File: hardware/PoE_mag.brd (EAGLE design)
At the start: 149.9 x 124.5 mm, 126 parts, among them IC1 LD1117V33, IC10 74LVC1T45SOT23-HAND, IC11 74LVC1T45SOT23-HAND, IC12 PCA9517A, IC2 LD1117V33, IC3 DS1338, IC4 ATMEGA1284, IC5 TSR 1-2450, IC6 LM61, IC7 MCP2200, IC8 74LVC1T45SOT23-HAND, IC9 74LVC1T45SOT23-HAND, Q1 BSS138, Q2 BUK98150-55A, X1 PWR, X2 JTAG, X3 USB, X4 MICRO-SD-SOCKETHIROSE-DM3D, X5 CONN-SMATHD, X6 UFL, X7 22-23-2021, X8 RJ45, X9 RJ11, Y1 32k768, Y2 12MHz, Y3 12MHz

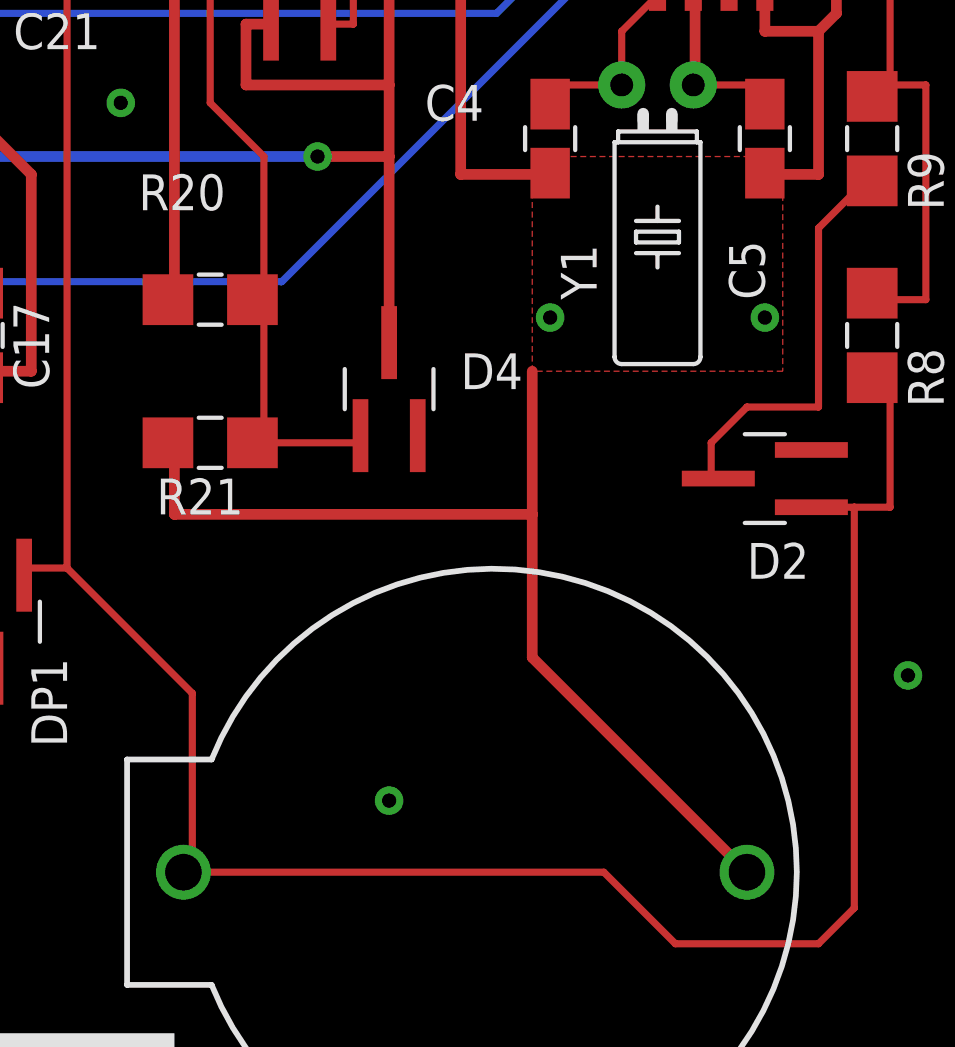
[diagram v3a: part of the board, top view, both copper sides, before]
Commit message: Add pads for support wire over 32768Hz crystal
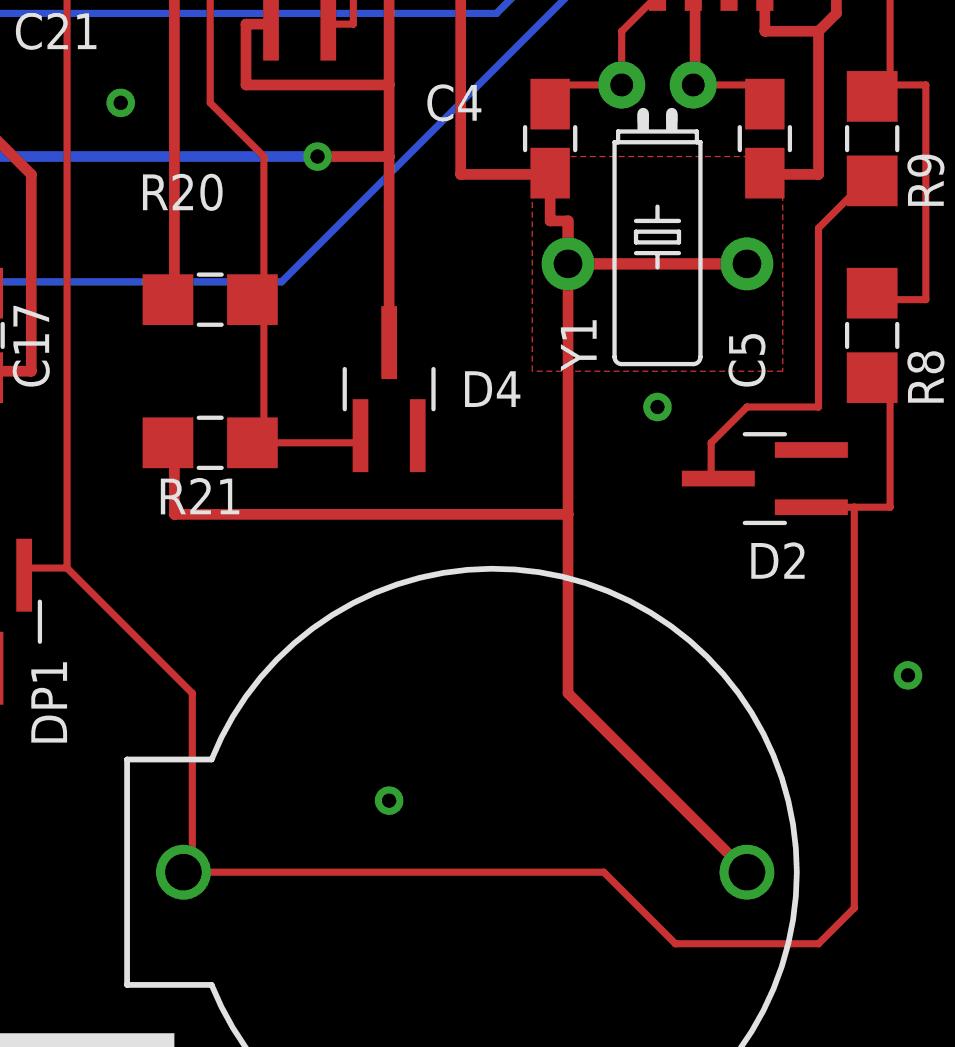
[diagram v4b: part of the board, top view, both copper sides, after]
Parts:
- added U$14, U$15: PAD, SteveMarple:PAD
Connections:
- net GND: now also U$14.1, U$15.1
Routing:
- net GND: track 1210.2 -> 1224.9 mm, vias 75 -> 74
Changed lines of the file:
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@@
 <rectangle x1="87.122" y1="1.524" x2="91.186" y2="2.794" layer="42"/>
 <text x="82.55" y="101.6" size="1.27" layer="25" ratio="10">PCB REV: 2</text>
+<wire x1="142.875" y1="24.765" x2="143.51" y2="23.495" width="0.254" layer="27"/>
+<wire x1="142.875" y1="24.765" x2="144.145" y2="23.495" width="0.254" layer="27"/>
+<wire x1="144.145" y1="24.13" x2="142.875" y2="24.765" width="0.254" layer="27"/>
+<wire x1="143.51" y1="23.495" x2="144.145" y2="24.13" width="0.254" layer="27"/>
+<wire x1="144.145" y1="23.495" x2="144.145" y2="22.225" width="0.254" layer="27"/>
 </plain>
 <attributes>
@@
 </class>
 </classes>
-<designrules name="SparkFun_Iteadstudio_10_12mil *">
+<designrules name="SparkFun_Iteadstudio_10_12mil">
 <description language="en">&lt;b&gt;EAGLE Design Rules&lt;/b&gt;
 &lt;p&gt;
@@
 </element>
 <element name="Y1" library="SteveMarple" package="TC38H" value="32k768" x="139.065" y="29.21" smashed="yes" rot="R180">
-<attribute name="NAME" x="136.906" y="21.59" size="1.27" layer="25" ratio="10" rot="R90"/>
+<attribute name="NAME" x="136.906" y="19.05" size="1.27" layer="25" ratio="10" rot="R90"/>
 </element>
 <element name="R2" library="SteveMarple" package="1206-HAND" value="560R" x="45.72" y="88.9" smashed="yes" rot="R270">
@@
 </element>
 <element name="C5" library="SteveMarple" package="0805-HAND" value="15p" x="142.875" y="27.305" smashed="yes" rot="R270">
-<attribute name="NAME" x="142.875" y="21.59" size="1.27" layer="25" ratio="10" rot="R90"/>
-<attribute name="VALUE" x="144.78" y="21.59" size="1.27" layer="27" ratio="10" rot="R90"/>
+<attribute name="NAME" x="142.875" y="18.415" size="1.27" layer="25" ratio="10" rot="R90"/>
+<attribute name="VALUE" x="144.78" y="18.415" size="1.27" layer="27" ratio="10" rot="R90"/>
 </element>
 <element name="C4" library="SteveMarple" package="0805-HAND" value="15p" x="135.255" y="27.305" smashed="yes" rot="R270">
@@
 </element>
 <element name="D4" library="SteveMarple" package="SOT23-3-HAND" value="BAS40" x="129.54" y="18.415" smashed="yes" rot="R90">
-<attribute name="NAME" x="132.08" y="18.415" size="1.27" layer="25" ratio="10" rot="SR0"/>
-<attribute name="VALUE" x="132.08" y="17.78" size="1.016" layer="27" ratio="10" rot="SR0" align="top-left"/>
+<attribute name="NAME" x="132.08" y="17.78" size="1.27" layer="25" ratio="10" rot="SR0"/>
+<attribute name="VALUE" x="132.08" y="16.51" size="1.016" layer="27" ratio="10" rot="SR0" align="top-left"/>
 </element>
 <element name="C41" library="SteveMarple" package="1206-HAND" value="100n" x="34.29" y="68.58" smashed="yes" rot="R270">
@@
 <attribute name="VALUE" x="72.39" y="10.16" size="1.27" layer="27" ratio="10"/>
 </element>
+<element name="U$14" library="SteveMarple" package="PAD" value="PAD" x="142.24" y="22.86"/>
+<element name="U$15" library="SteveMarple" package="PAD" value="PAD" x="135.89" y="22.86"/>
 </elements>
 <signals>
@@
 <wire x1="121.92" y1="16.51" x2="121.793" y2="16.637" width="0.381" layer="1"/>
 <wire x1="121.92" y1="13.97" x2="121.92" y2="16.51" width="0.381" layer="1"/>
-<wire x1="134.62" y1="13.97" x2="121.92" y2="13.97" width="0.381" layer="1"/>
-<wire x1="134.62" y1="19.05" x2="134.62" y2="13.97" width="0.381" layer="1"/>
+<wire x1="135.89" y1="13.97" x2="121.92" y2="13.97" width="0.381" layer="1"/>
+<wire x1="135.89" y1="22.86" x2="135.89" y2="13.97" width="0.381" layer="1"/>
 <wire x1="121.92" y1="16.51" x2="121.691" y2="16.51" width="0.381" layer="1"/>
 <wire x1="132.08" y1="33.655" x2="136.525" y2="33.655" width="0.381" layer="1"/>
@@
 <wire x1="132.08" y1="26.035" x2="132.08" y2="33.655" width="0.381" layer="1"/>
 <wire x1="135.128" y1="26.162" x2="135.255" y2="26.035" width="0.381" layer="1"/>
+<wire x1="135.255" y1="26.035" x2="135.255" y2="24.384" width="0.381" layer="1"/>
+<wire x1="135.255" y1="24.384" x2="135.89" y2="24.384" width="0.381" layer="1"/>
 <wire x1="135.255" y1="26.035" x2="132.08" y2="26.035" width="0.381" layer="1"/>
 <wire x1="136.398" y1="34.036" x2="136.525" y2="34.061" width="0.381" layer="1"/>
@@
 <wire x1="142.875" y1="26.035" x2="144.78" y2="26.035" width="0.381" layer="1"/>
 <wire x1="143.002" y1="26.162" x2="142.875" y2="26.08" width="0.381" layer="1"/>
-<wire x1="134.62" y1="8.89" x2="142.24" y2="1.27" width="0.381" layer="1"/>
-<wire x1="134.62" y1="13.97" x2="134.62" y2="8.89" width="0.381" layer="1"/>
+<wire x1="135.89" y1="7.62" x2="142.24" y2="1.27" width="0.381" layer="1"/>
+<wire x1="135.89" y1="13.97" x2="135.89" y2="7.62" width="0.381" layer="1"/>
 <wire x1="132.08" y1="33.655" x2="126.365" y2="33.655" width="0.381" layer="16"/>
 <wire x1="60.96" y1="24.765" x2="61.366" y2="24.765" width="0.6096" layer="1"/>
@@
 <via x="140.335" y="60.325" extent="1-16" drill="0.508"/>
 <via x="135.255" y="62.865" extent="1-16" drill="0.508"/>
-<via x="135.255" y="20.955" extent="1-16" drill="0.508"/>
-<via x="142.875" y="20.955" extent="1-16" drill="0.508"/>
 <via x="113.03" y="19.05" extent="1-16" drill="0.508"/>
 <via x="31.75" y="63.5" extent="1-16" drill="0.508"/>
@@
 <wire x1="63.5" y1="96.52" x2="63.754" y2="96.52" width="0.381" layer="1"/>
 <via x="102.87" y="101.6" extent="1-16" drill="0.508"/>
+<via x="139.065" y="17.78" extent="1-16" drill="0.508"/>
+<contactref element="U$14" pad="1"/>
+<contactref element="U$15" pad="1"/>
+<wire x1="142.24" y1="22.86" x2="135.89" y2="22.86" width="0.4064" layer="1"/>
+<wire x1="135.89" y1="22.86" x2="135.89" y2="24.384" width="0.4064" layer="1"/>
 </signal>
 <signal name="VCC" class="1">

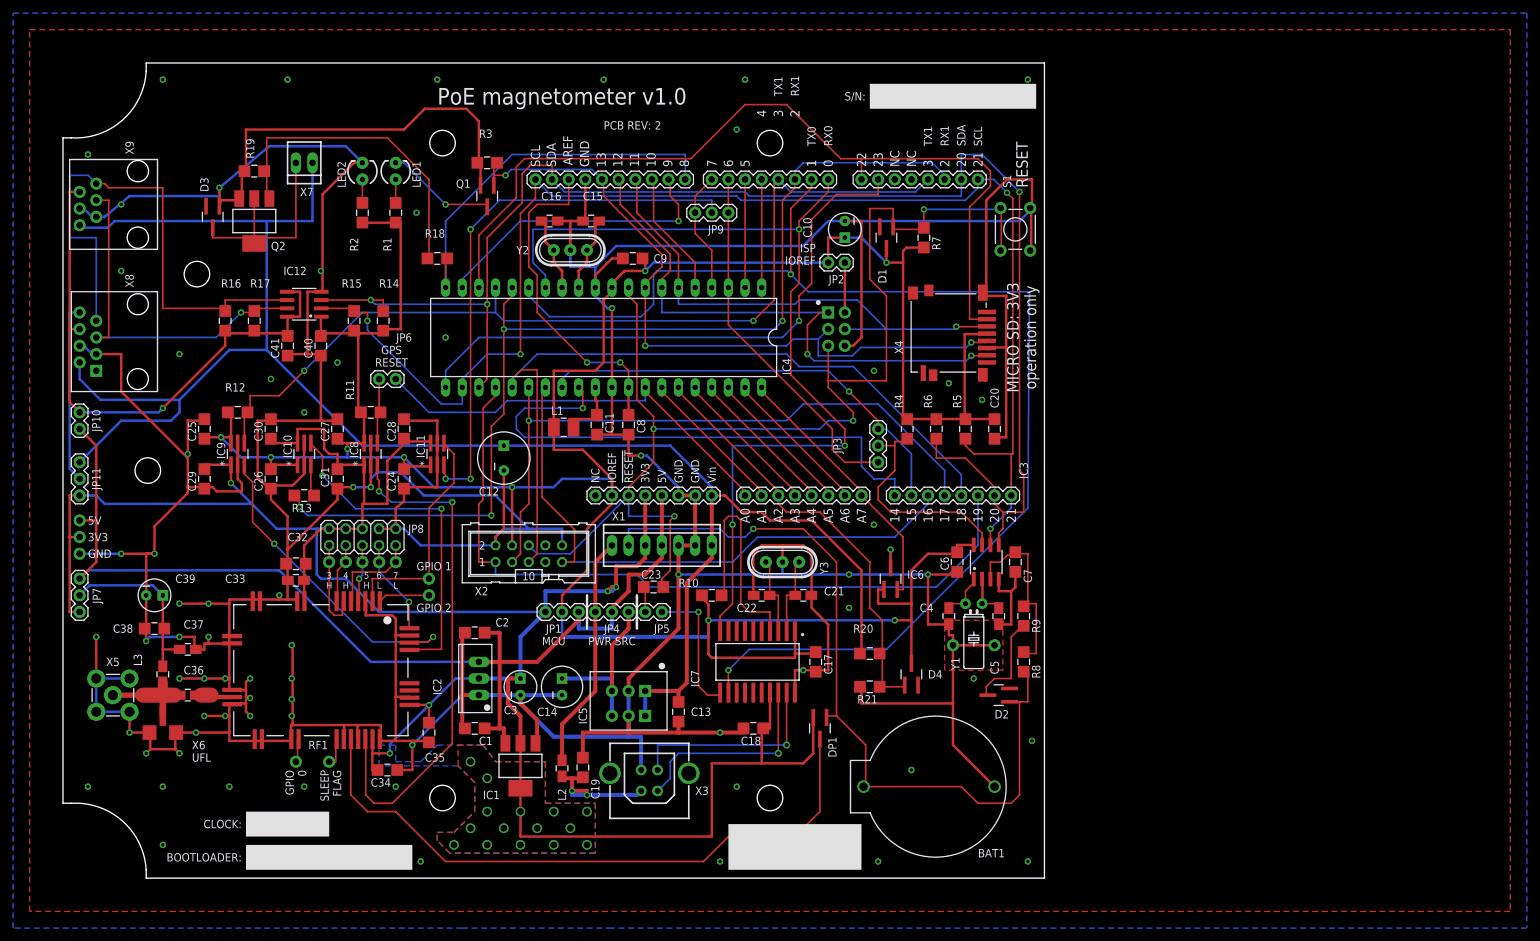
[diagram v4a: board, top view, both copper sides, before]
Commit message: Reroute bottom layer tracks to avoid lugs on box
Also use 4mm diameter mounting holes
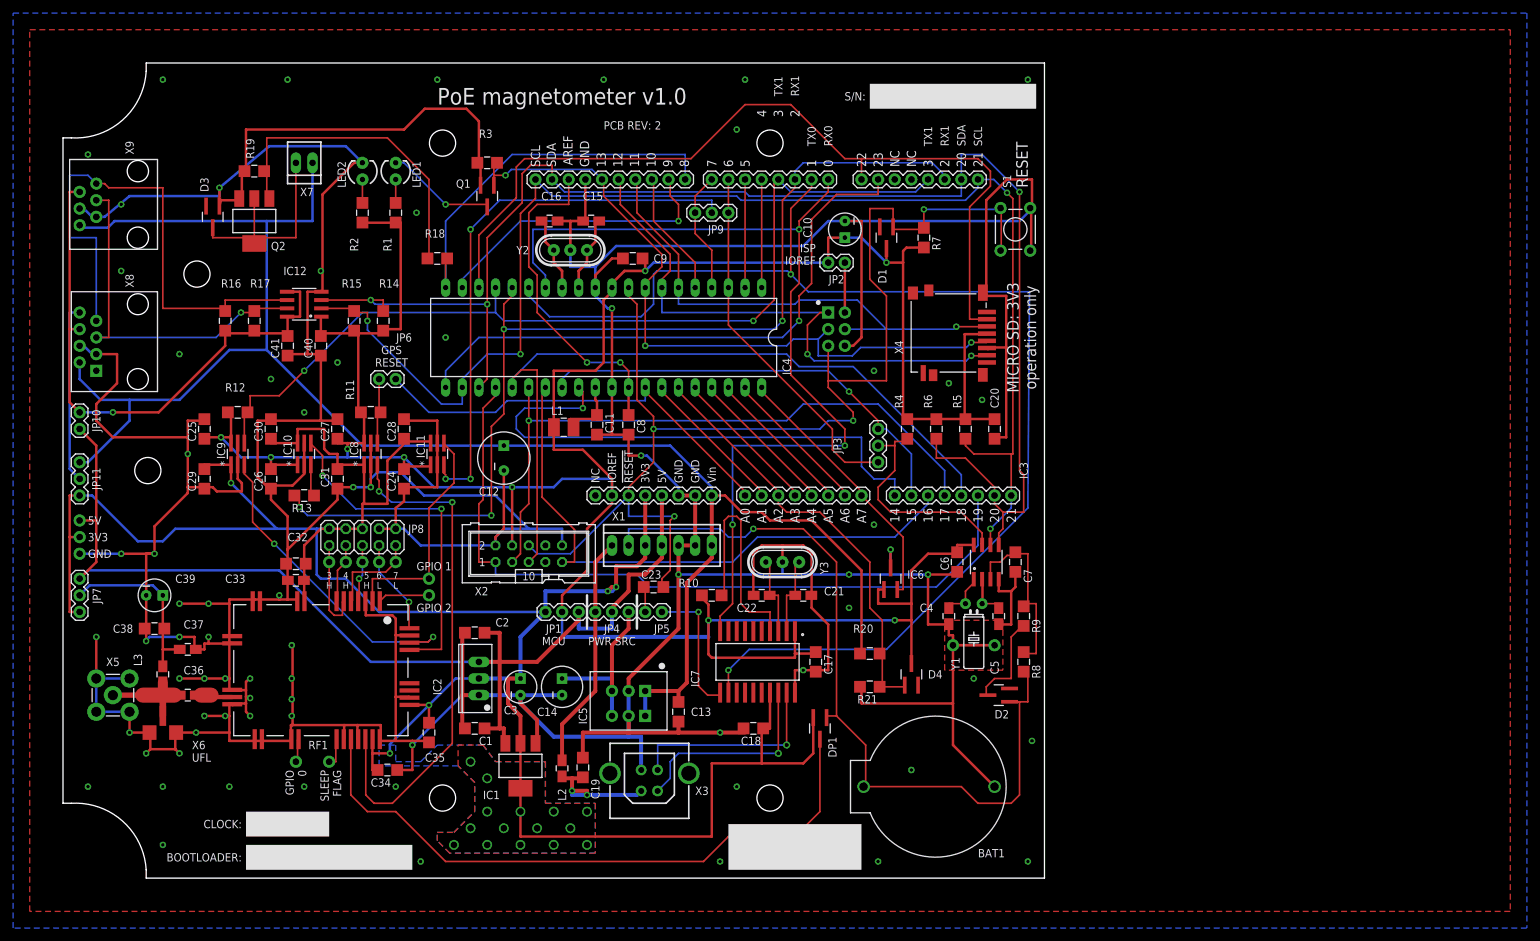
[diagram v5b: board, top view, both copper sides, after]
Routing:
- net +3V3: track 375.6 -> 382.6 mm
- net VIN: track 278.1 -> 271.2 mm
- net GND: track 1224.9 -> 1230.7 mm
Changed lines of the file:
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@@
 <wire x1="27.305" y1="47.625" x2="27.305" y2="46.355" width="0.381" layer="1"/>
 <wire x1="19.05" y1="57.15" x2="21.59" y2="57.15" width="0.381" layer="1"/>
-<wire x1="19.05" y1="46.99" x2="19.05" y2="51.435" width="0.381" layer="1"/>
-<wire x1="19.05" y1="51.435" x2="19.05" y2="57.15" width="0.381" layer="1"/>
+<wire x1="19.05" y1="46.99" x2="19.05" y2="54.61" width="0.381" layer="1"/>
+<wire x1="19.05" y1="54.61" x2="19.05" y2="57.15" width="0.381" layer="1"/>
 <wire x1="19.05" y1="46.99" x2="19.05" y2="46.101" width="0.381" layer="1"/>
 <wire x1="21.59" y1="57.15" x2="21.59" y2="57.379" width="0.381" layer="1"/>
 <wire x1="26.67" y1="50.419" x2="26.67" y2="53.721" width="0.381" layer="1"/>
-<wire x1="8.89" y1="67.31" x2="5.08" y2="67.31" width="0.381" layer="1"/>
-<wire x1="8.89" y1="61.595" x2="8.89" y2="67.31" width="0.381" layer="1"/>
-<wire x1="19.05" y1="51.435" x2="8.89" y2="61.595" width="0.381" layer="1"/>
+<wire x1="8.255" y1="67.31" x2="5.08" y2="67.31" width="0.381" layer="1"/>
+<wire x1="7.62" y1="54.61" x2="5.08" y2="57.15" width="0.381" layer="1"/>
+<wire x1="5.08" y1="57.15" x2="5.08" y2="59.69" width="0.381" layer="1"/>
+<wire x1="5.08" y1="59.69" x2="8.255" y2="62.865" width="0.381" layer="1"/>
+<wire x1="8.255" y1="62.865" x2="8.255" y2="67.31" width="0.381" layer="1"/>
+<wire x1="19.05" y1="54.61" x2="7.62" y2="54.61" width="0.381" layer="1"/>
 <wire x1="13.97" y1="36.83" x2="8.89" y2="36.83" width="0.381" layer="1"/>
 <wire x1="13.97" y1="36.83" x2="13.97" y2="41.021" width="0.381" layer="1"/>
@@
 <wire x1="95.885" y1="97.155" x2="70.485" y2="97.155" width="0.254" layer="1"/>
 <wire x1="104.14" y1="105.41" x2="95.885" y2="97.155" width="0.254" layer="1"/>
-<wire x1="121.92" y1="97.155" x2="118.745" y2="97.155" width="0.254" layer="1"/>
-<wire x1="118.745" y1="97.155" x2="110.49" y2="105.41" width="0.254" layer="1"/>
-<wire x1="110.49" y1="105.41" x2="104.14" y2="105.41" width="0.254" layer="1"/>
+<wire x1="121.92" y1="97.155" x2="119.38" y2="97.155" width="0.254" layer="1"/>
+<wire x1="119.38" y1="97.155" x2="111.125" y2="105.41" width="0.254" layer="1"/>
+<wire x1="111.125" y1="105.41" x2="104.14" y2="105.41" width="0.254" layer="1"/>
 </signal>
 <signal name="9">
@@
 <wire x1="43.18" y1="40.64" x2="45.72" y2="40.64" width="0.381" layer="1"/>
 <wire x1="25.654" y1="47.625" x2="25.654" y2="50.419" width="0.381" layer="1"/>
-<wire x1="32.639" y1="40.64" x2="28.829" y2="44.45" width="0.381" layer="16"/>
-<wire x1="28.829" y1="44.45" x2="25.654" y2="47.625" width="0.381" layer="16"/>
+<wire x1="32.639" y1="40.64" x2="25.654" y2="47.625" width="0.381" layer="16"/>
 <wire x1="40.64" y1="40.64" x2="38.735" y2="40.64" width="0.381" layer="16"/>
 <wire x1="38.735" y1="40.64" x2="32.639" y2="40.64" width="0.381" layer="16"/>
@@
 <wire x1="36.83" y1="38.1" x2="36.83" y2="35.56" width="0.381" layer="1"/>
 <wire x1="36.83" y1="35.56" x2="37.059" y2="35.306" width="0.381" layer="1"/>
-<wire x1="28.829" y1="44.45" x2="6.35" y2="44.45" width="0.381" layer="16"/>
-<wire x1="6.35" y1="44.45" x2="5.08" y2="45.72" width="0.381" layer="16"/>
-<wire x1="5.08" y1="45.72" x2="2.54" y2="45.72" width="0.381" layer="16"/>
+<wire x1="32.639" y1="40.64" x2="17.145" y2="40.64" width="0.381" layer="16"/>
+<wire x1="17.145" y1="40.64" x2="15.24" y2="38.735" width="0.381" layer="16"/>
+<wire x1="15.24" y1="38.735" x2="11.43" y2="38.735" width="0.381" layer="16"/>
+<wire x1="11.43" y1="38.735" x2="4.445" y2="45.72" width="0.381" layer="16"/>
+<wire x1="4.445" y1="45.72" x2="2.54" y2="45.72" width="0.381" layer="16"/>
 <wire x1="113.03" y1="4.826" x2="114.554" y2="6.35" width="0.381" layer="1"/>
 <wire x1="106.68" y1="4.826" x2="113.03" y2="4.826" width="0.381" layer="1"/>
@@
 <wire x1="99.06" y1="38.1" x2="99.06" y2="36.195" width="0.6096" layer="1"/>
 <wire x1="99.06" y1="36.195" x2="95.25" y2="32.385" width="0.6096" layer="1"/>
-<wire x1="8.89" y1="57.15" x2="2.54" y2="50.8" width="0.381" layer="16"/>
-<wire x1="16.51" y1="57.15" x2="8.89" y2="57.15" width="0.381" layer="16"/>
-<wire x1="17.78" y1="58.42" x2="16.51" y2="57.15" width="0.381" layer="16"/>
-<wire x1="17.78" y1="60.325" x2="17.78" y2="58.42" width="0.381" layer="16"/>
-<wire x1="5.715" y1="60.325" x2="17.78" y2="60.325" width="0.381" layer="16"/>
+<wire x1="10.16" y1="57.15" x2="3.81" y2="50.8" width="0.381" layer="16"/>
+<wire x1="3.81" y1="50.8" x2="2.54" y2="50.8" width="0.381" layer="16"/>
+<wire x1="10.16" y1="60.325" x2="10.16" y2="57.15" width="0.381" layer="16"/>
+<wire x1="5.715" y1="60.325" x2="10.16" y2="60.325" width="0.381" layer="16"/>
+<wire x1="10.16" y1="60.325" x2="17.78" y2="60.325" width="0.381" layer="16"/>
 <wire x1="2.54" y1="63.5" x2="5.715" y2="60.325" width="0.381" layer="16"/>
 <wire x1="2.54" y1="66.04" x2="2.54" y2="63.5" width="0.381" layer="16"/>
@@
 <wire x1="1.016" y1="71.12" x2="1.016" y2="92.075" width="0.381" layer="1"/>
 <wire x1="1.016" y1="92.075" x2="2.54" y2="92.075" width="0.381" layer="1"/>
-<wire x1="15.24" y1="59.055" x2="24.765" y2="68.58" width="0.381" layer="1"/>
+<wire x1="7.62" y1="58.42" x2="14.605" y2="58.42" width="0.381" layer="1"/>
+<wire x1="14.605" y1="58.42" x2="24.765" y2="68.58" width="0.381" layer="1"/>
 <wire x1="24.765" y1="68.58" x2="24.765" y2="70.866" width="0.381" layer="1"/>
-<wire x1="14.605" y1="58.42" x2="15.24" y2="59.055" width="0.381" layer="16"/>
-<wire x1="2.54" y1="58.42" x2="14.605" y2="58.42" width="0.381" layer="16"/>
+<wire x1="2.54" y1="58.42" x2="7.62" y2="58.42" width="0.381" layer="16"/>
 <wire x1="24.765" y1="70.866" x2="24.765" y2="70.891" width="0.381" layer="1"/>
-<via x="15.24" y="59.055" extent="1-16" drill="0.508"/>
+<via x="7.62" y="58.42" extent="1-16" drill="0.508"/>
 </signal>
 <signal name="MAG_SCL">
